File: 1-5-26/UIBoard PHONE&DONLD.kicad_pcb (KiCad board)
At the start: 4 copper layers, 355 x 255 mm, 84 parts, among them J1 XT60-M, J2 XT60-M, J5 M22-7130442, J7 22035035, Q1 2N3904, Q2 2N3904, Q3 2N3904, Q4 2N3904, SW1 A8L-11-12N1, U1 UA78M05-Q1, U2 MCP2562-E-P, U3 CD4511BPWR, U5 7 Segment Display, U6 STM32 Nucleo F446RE, U7 PCF8574AP

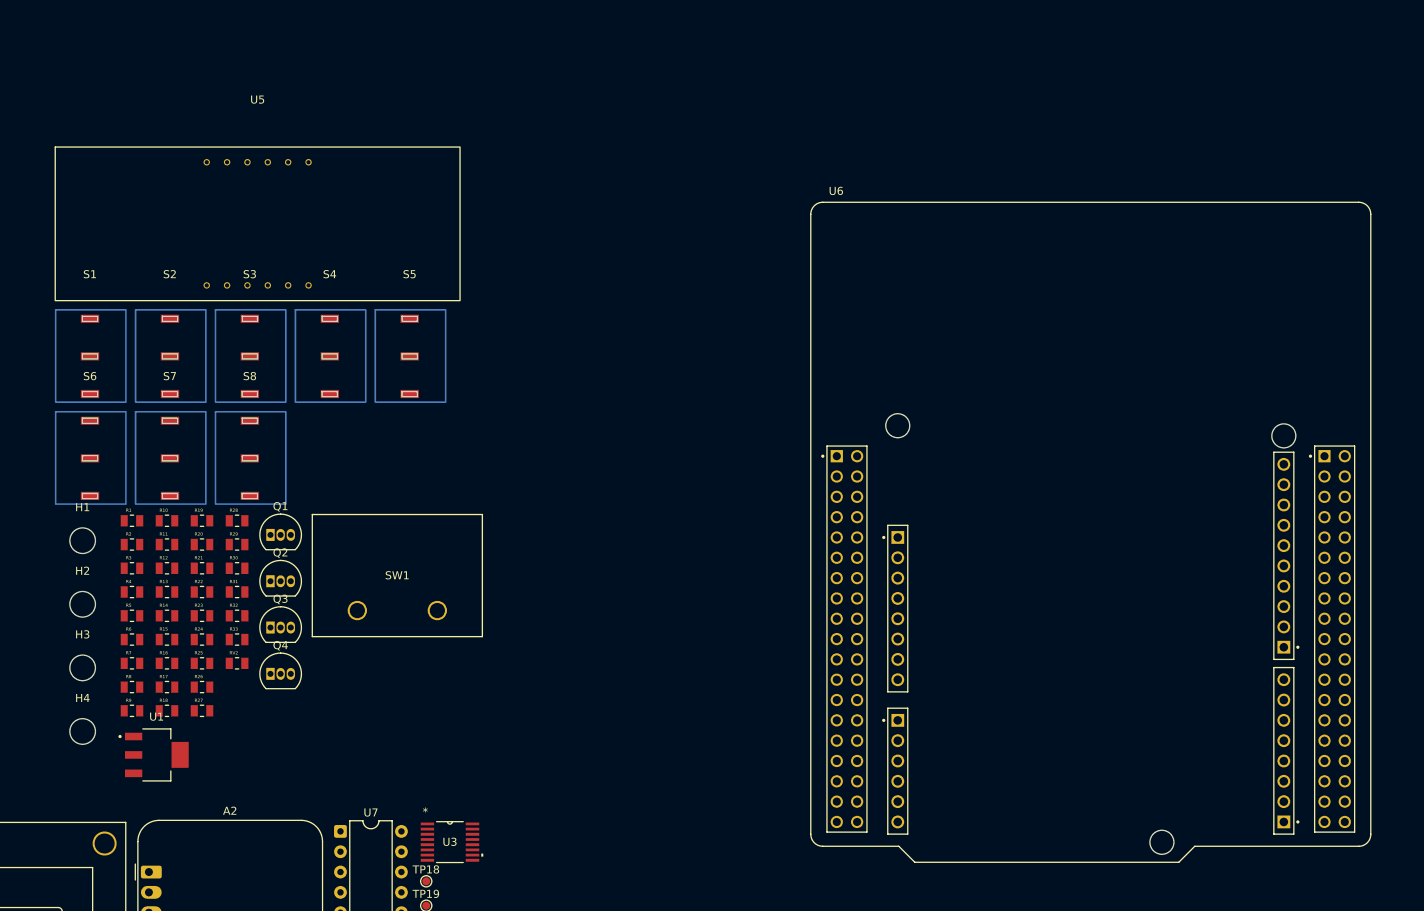
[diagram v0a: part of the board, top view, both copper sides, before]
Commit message: Fixed nets for STM32 and 7 Segment Display
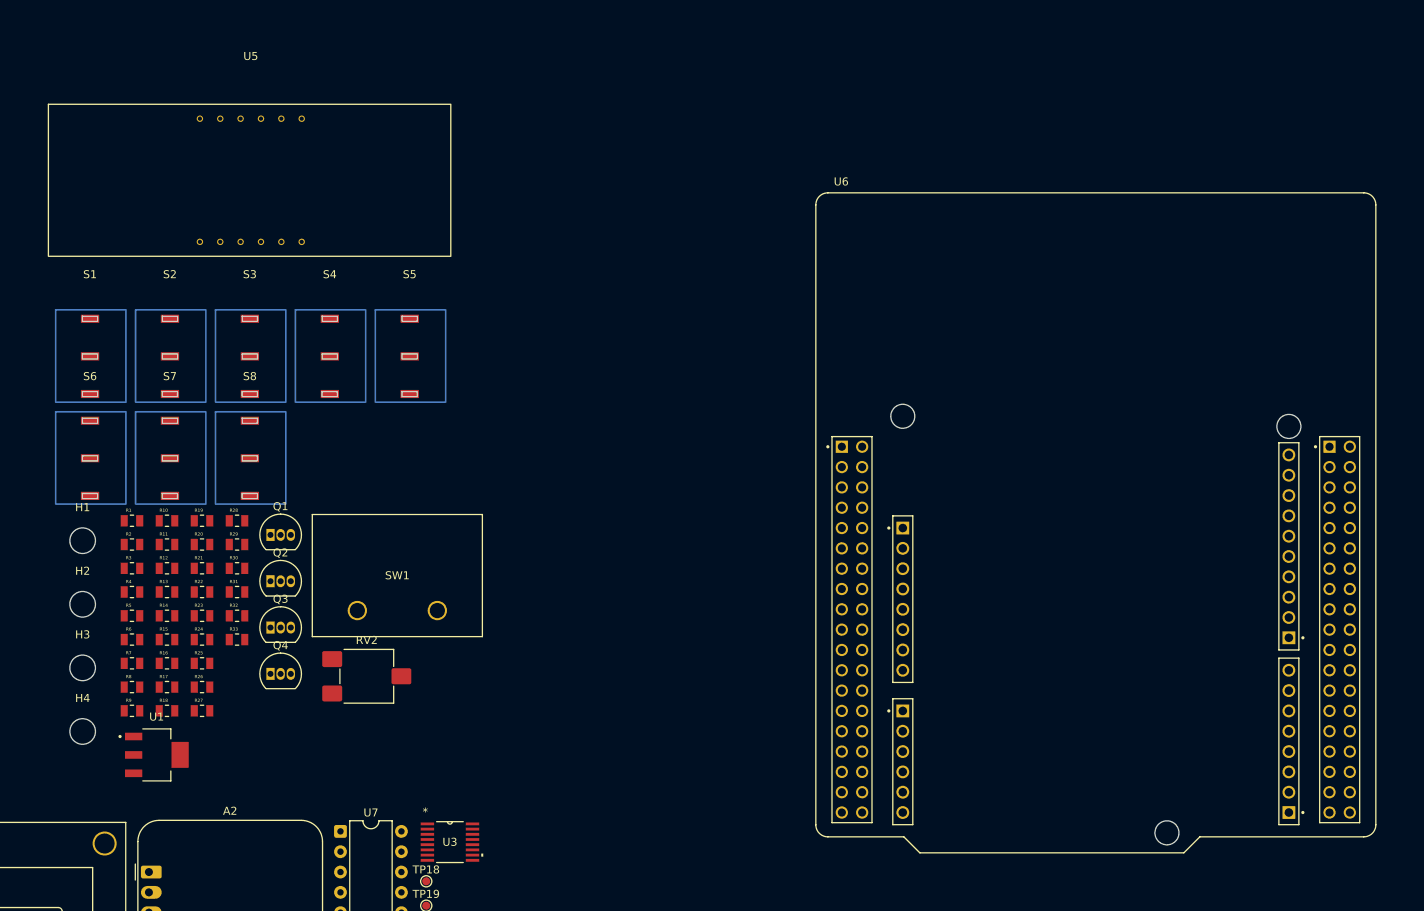
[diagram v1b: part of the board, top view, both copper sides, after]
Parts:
- RV2: footprint SMV_Passives:0805RESC2012X60N -> Potentiometer_SMD:Potentiometer_ACP_CA6-VSMD_Vertical
- moved RV2 16.3 mm to (129.5, 86.0)
- moved U5 5.51 mm to (115.0, 24.0)
- moved U6 1.34 mm to (220.6, 66.8)
